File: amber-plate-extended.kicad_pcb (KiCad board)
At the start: 2 copper layers, 127 x 119.3 mm, 6 parts

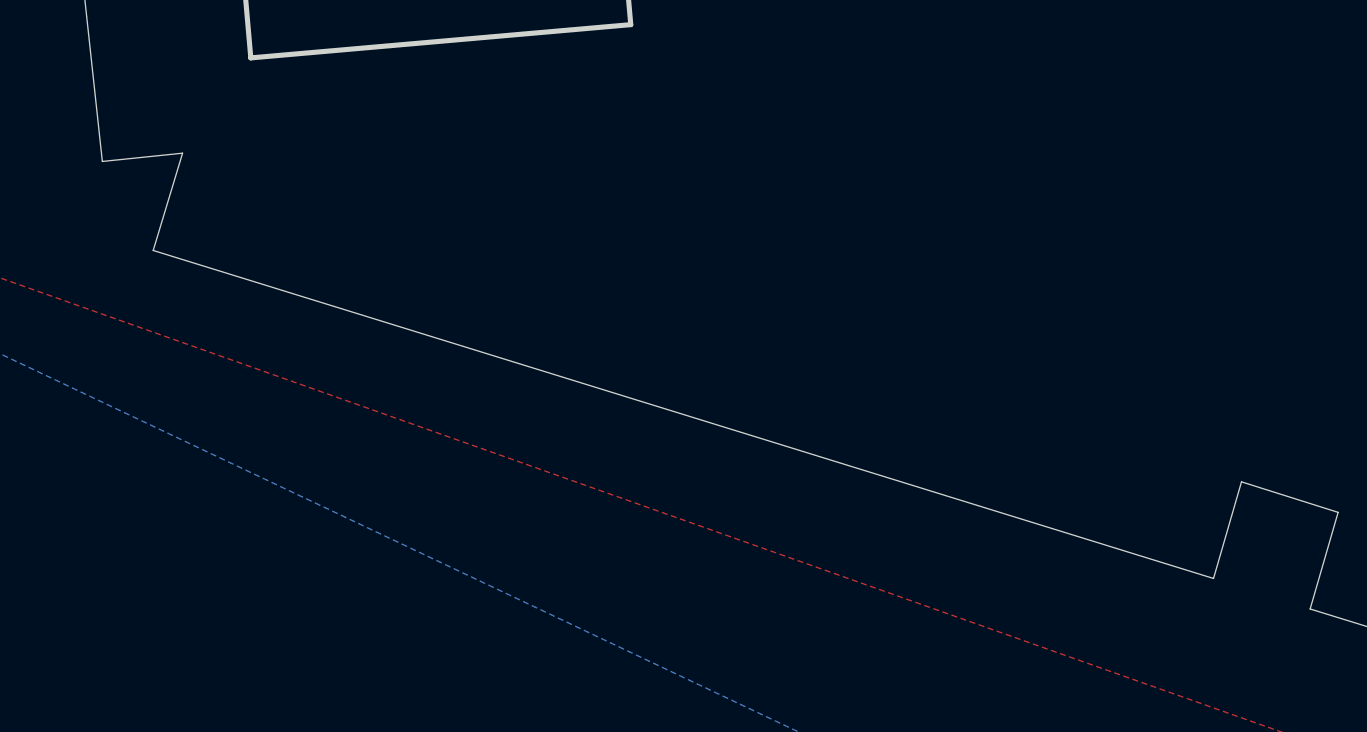
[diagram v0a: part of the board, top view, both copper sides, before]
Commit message: Create gerbers for v2
Also shorten a gasket mount flap a bit in extended plate
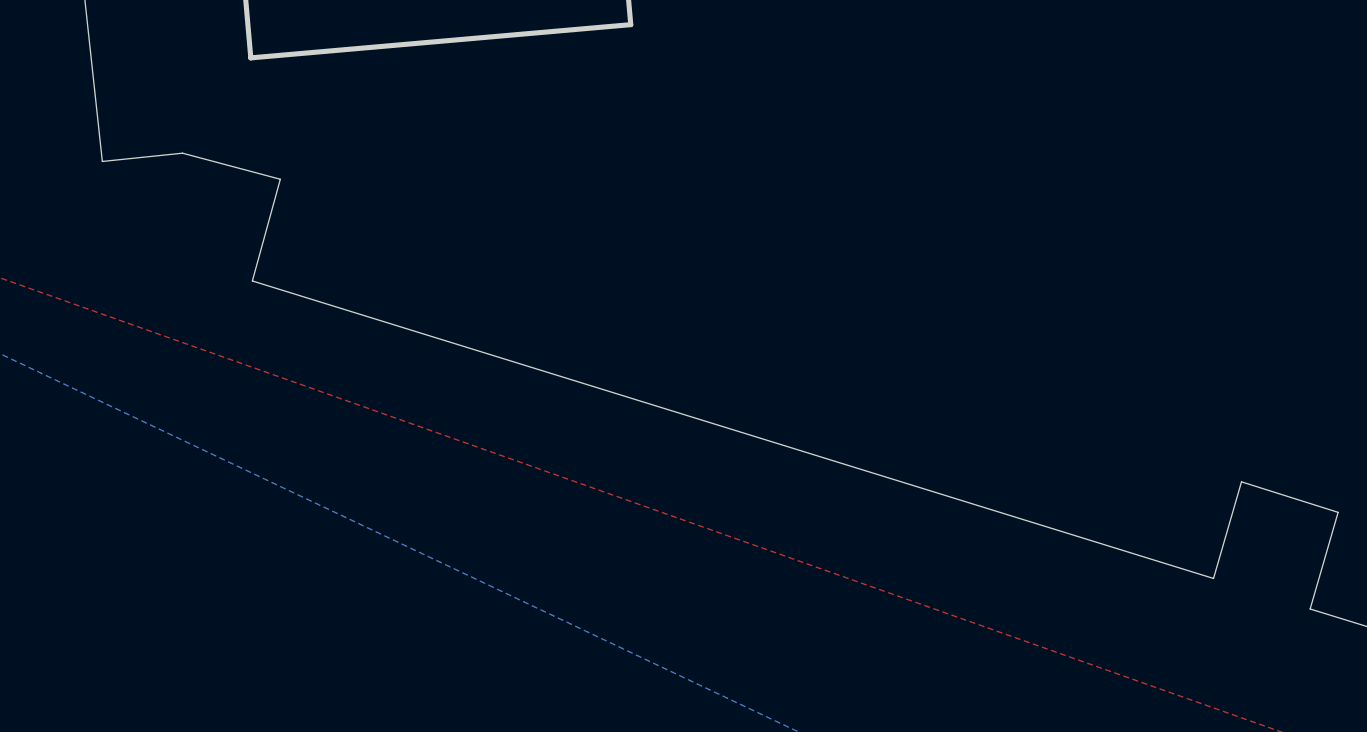
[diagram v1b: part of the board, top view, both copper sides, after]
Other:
- outline, holes or cut-outs redrawn
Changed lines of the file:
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@@
   (general
     (thickness 1.6)
-    (drawings 259)
+    (drawings 260)
     (tracks 0)
     (zones 0)
@@
       (effects (font (size 1 1) (thickness 0.15)))
     )
+    (fp_circle (center 0 0) (end 5.3 0) (layer Cmts.User) (width 0.15))
     (fp_circle (center 0 0) (end 5.55 0) (layer F.CrtYd) (width 0.05))
-    (fp_circle (center 0 0) (end 5.3 0) (layer Cmts.User) (width 0.15))
     (fp_text user %R (at 0.3 0) (layer F.Fab)
       (effects (font (size 1 1) (thickness 0.15)))
@@
     (pad "" thru_hole circle (at 0 0) (size 4.2 4.2) (drill 2.3) (layers *.Cu *.Mask))
   )
+  (gr_line (start -5.7 12.4) (end -6.8 16.4) (layer Edge.Cuts) (width 0.05))
+  (gr_line (start -9.544909 11.375179) (end -5.7 12.4) (layer Edge.Cuts) (width 0.05))
   (gr_line (start 105.9 26.5) (end 110 26.5) (layer Edge.Cuts) (width 0.05))
   (gr_line (start 105.81798 30.4) (end 105.9 26.5) (layer Edge.Cuts) (width 0.05))
@@
   (gr_line (start 32.1 24.3) (end 35.9 25.5) (layer Edge.Cuts) (width 0.05))
   (gr_line (start 31 28.1) (end 32.1 24.3) (layer Edge.Cuts) (width 0.05))
-  (gr_line (start -10.7 15.2) (end 31 28.1) (layer Edge.Cuts) (width 0.05))
-  (gr_line (start -9.544909 11.375179) (end -10.7 15.2) (layer Edge.Cuts) (width 0.05))
+  (gr_line (start -6.8 16.4) (end 31 28.1) (layer Edge.Cuts) (width 0.05))
   (gr_line (start -12.7 11.7) (end -9.544909 11.375179) (layer Edge.Cuts) (width 0.05))
   (gr_line (start -17 -28.1) (end -12.7 11.7) (layer Edge.Cuts) (width 0.05))
